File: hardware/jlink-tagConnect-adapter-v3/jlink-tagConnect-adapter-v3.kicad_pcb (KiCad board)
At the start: 2 copper layers, 48.3 x 30.5 mm, 15 parts, among them J1 Conn_02x10_Odd_Even, J2 Conn_02x05_Odd_Even, J3 Conn_02x05_Odd_Even, J4 Conn_01x03

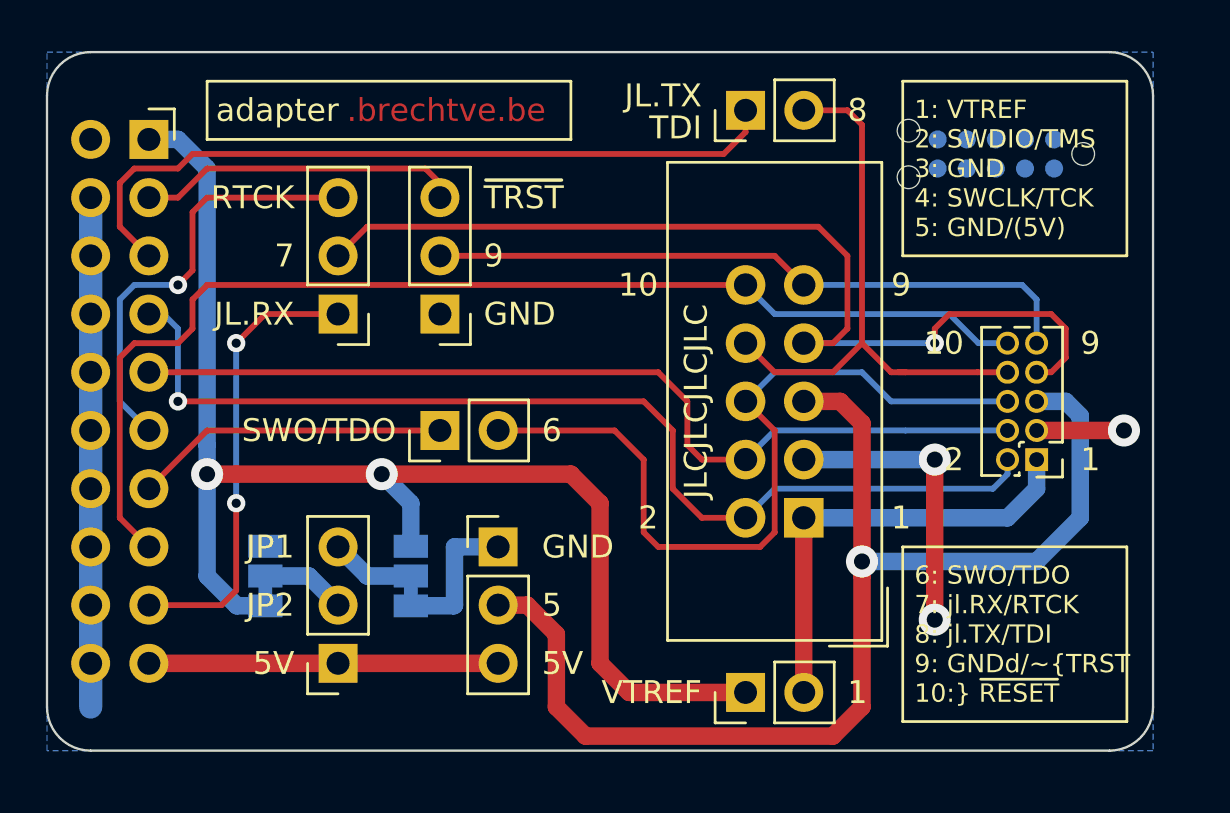
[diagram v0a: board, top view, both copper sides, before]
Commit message: Added 2x7 1.27mm Pinheader
(see STM32 STDC14 debug connector which uses the outer pins for UART)
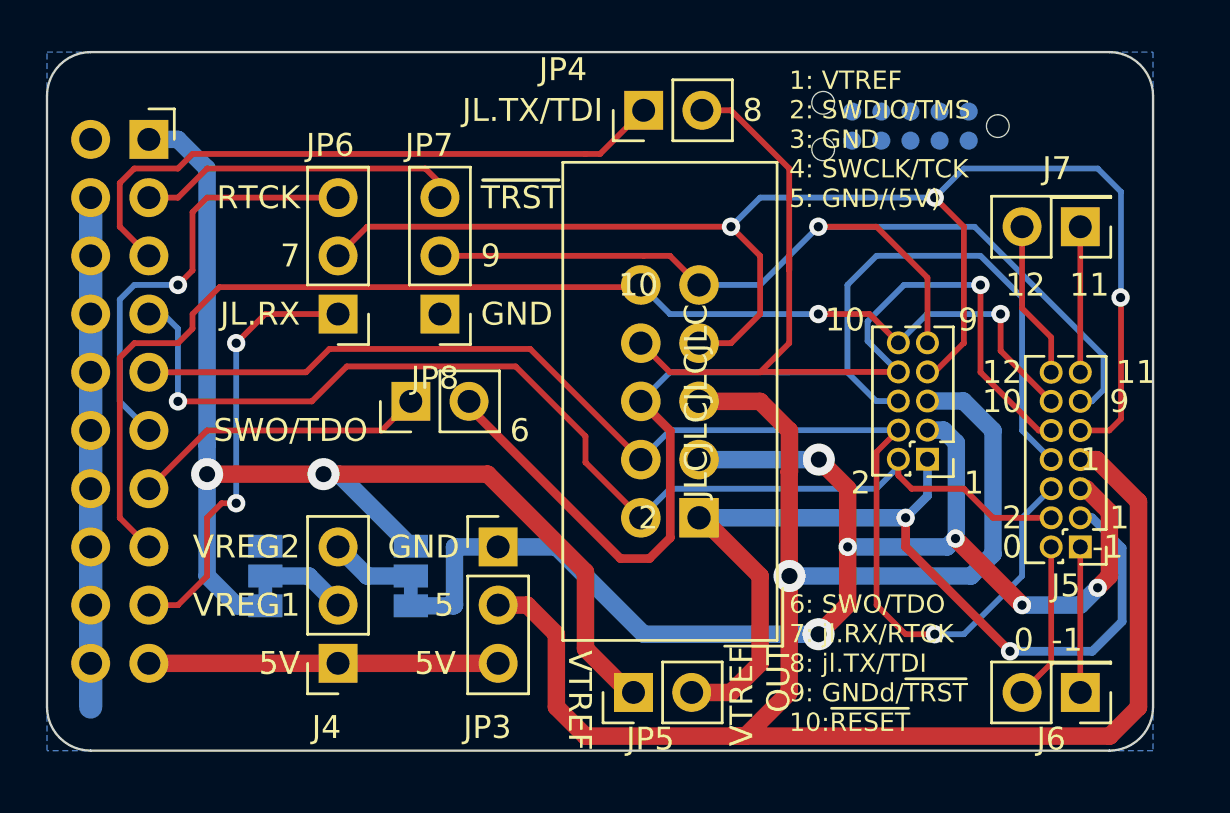
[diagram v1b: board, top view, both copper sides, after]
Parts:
- removed G1: Symbol_OSHW-Logo_11.4x12mm, BrechtVE_Aesthetics:OSHW-Logo_5.7x6mm_SolderMask
- added J5: Conn_02x07_Odd_Even, Connector_PinHeader_1.27mm:PinHeader_2x07_P1.27mm_Vertical, F.Cu at (134.6, 113.0)
- added J6: Conn_02x02_Odd_Even, Connector_PinHeader_2.54mm:PinHeader_2x01_P2.54mm_Vertical, F.Cu at (134.6, 119.4)
- added J7: Conn_02x02_Odd_Even, Connector_PinHeader_2.54mm:PinHeader_2x01_P2.54mm_Vertical, F.Cu at (134.6, 99.1)
- moved JP5 4.89 mm to (115.1, 119.4)
- moved J3 4.76 mm to (128.0, 109.2)
- moved J2 4.57 mm to (118.0, 111.8)
- moved JP4 4.45 mm to (115.6, 94.0)
- moved REF** 3.92 mm to (127.2, 94.7)
- moved JP8 1.80 mm to (105.4, 106.7)
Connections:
- net /~RESET renamed /~{RESET}
- net /~TRST renamed /~{TRST}
- J1 pad 2: (no net) -> unconnected-(J1-Pin_2-Pad2)
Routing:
- net /GND: track 45.1 -> 83.0 mm, vias 3 -> 6
- net PIN5: track 52.9 -> 82.3 mm
- net /VTREF-OUT: track 19.6 -> 41.7 mm, vias 0 -> 2
- net PIN7: track 45.3 -> 65.2 mm, vias 1 -> 3
- net PIN8: track 25.7 -> 43.0 mm, vias 0 -> 1
- net PIN6: track 35.0 -> 51.9 mm
- net PIN9: track 28.7 -> 44.1 mm, vias 0 -> 1
- net /SWCLK-TCK: track 40.7 -> 55.9 mm, vias 0 -> 1
- net PIN12: track 0.00 -> 6.88 mm
- net PIN0: track 0.00 -> 6.88 mm
- net PIN11: track 0.00 -> 6.35 mm
- net PIN-1: track 0.00 -> 6.35 mm
- net /VTREF: track 59.1 -> 53.3 mm
- net /TXD-TDI: track 32.9 -> 27.9 mm
- net /~{RESET}: track 50.6 -> 55.2 mm, vias 0 -> 2
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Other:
- net class Default removed
- board text added: "-1"
- board text added: "0"
- board text added: "11"
- board text added: "12"
- board text added: "6: SWO/TDO 7: jl.RX/RTCK 8: jl.TX/TDI 9: GNDd/~{TRST} 10:~{RESET}"
- board text added: "J4"
- board text added: "JL.TX/TDI"
- board text added: "JP3"
- board text added: "JP4"
- board text added: "JP5"
- board text added: "JP6"
- board text added: "JP7"
- board text added: "JP8"
- board text added: "VREG1"
- board text added: "VREG2"
- board text added: "VTREF OUT"
- board text added: "~{TRST}"
- board text removed: ".brechtve.be"
- board text removed: "11/2020"
- board text removed: "6: SWO/TDO 7: jl.RX/RTCK 8: jl.TX/TDI 9: GNDd/~TRST 10: ~RESET"
- board text removed: "JL.TX"
- board text removed: "JP1"
- board text removed: "JP2"
- board text removed: "Licensed under CERN OHL v.1.2"
- board text removed: "TDI"
- board text removed: "Universal J-Link Adapter"
- board text removed: "adapter"
- board text removed: "v3.0"
- board text removed: "~TRST"
